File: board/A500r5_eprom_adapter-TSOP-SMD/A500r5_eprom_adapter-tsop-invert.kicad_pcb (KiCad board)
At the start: 4 copper layers, 17.4 x 50.9 mm, 13 parts, among them J2 A18 Selector, J4 A17 Selector, U1 27C400-A500, U2 SST39SF040_TSOP, U3 SST39SF040_TSOP

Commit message: Update the README
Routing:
- net GND: track 65.7 -> 69.8 mm
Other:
- board text added: "Rev. 1"
- board text removed: "Rev. 0"
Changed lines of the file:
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@@
 		)
 	)
-	(gr_text "Rev. 0"
+	(gr_text "Rev. 1"
 		(at 112.268 124.206 90)
 		(layer "F.SilkS")
@@
 	)
 	(segment
-		(start 117.3124 112.9736)
-		(end 117.3124 115.7884)
+		(start 118.115 112.171)
+		(end 115.921 112.171)
 		(width 0.25)
 		(layer "F.Cu")
@@
 	)
 	(segment
-		(start 117.3124 115.7884)
-		(end 118.11 116.586)
+		(start 115.57 116.332)
+		(end 115.57 112.522)
 		(width 0.25)
 		(layer "F.Cu")
@@
 	)
 	(segment
-		(start 118.115 112.171)
-		(end 117.3124 112.9736)
+		(start 118.11 116.586)
+		(end 115.824 116.586)
 		(width 0.25)
 		(layer "F.Cu")
+		(net 1)
+	)
+	(segment
+		(start 115.824 116.586)
+		(end 115.57 116.332)
+		(width 0.25)
+		(layer "F.Cu")
+		(net 1)
+	)
+	(segment
+		(start 115.921 112.171)
+		(end 115.57 112.522)
+		(width 0.25)
+		(layer "F.Cu")

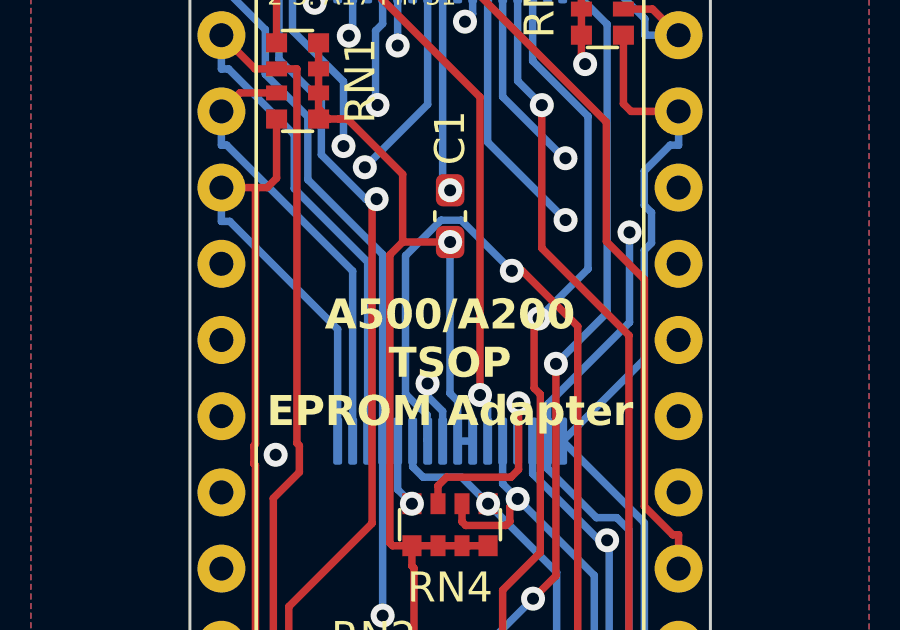
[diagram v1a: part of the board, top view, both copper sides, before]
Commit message: Fix "A2000" silkscreen in PLCC and TSOP adapter variants
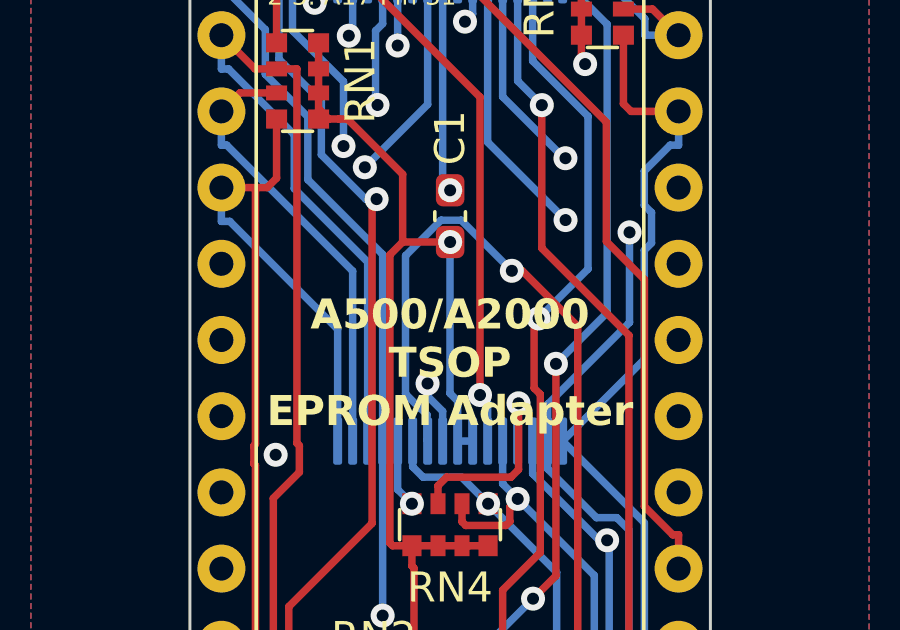
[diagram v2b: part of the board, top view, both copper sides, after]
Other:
- board text added: "A500/A2000 TSOP EPROM Adapter"
- board text removed: "A500/A200 TSOP EPROM Adapter"
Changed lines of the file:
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@@
 			(drillshape 0)
 			(scaleselection 1)
-			(outputdirectory "gerbers/rev0/")
+			(outputdirectory "gerbers/rev1/")
 		)
 	)
@@
 		)
 	)
-	(gr_text "A500/A200\nTSOP\nEPROM Adapter"
+	(gr_text "A500/A2000\nTSOP\nEPROM Adapter"
 		(at 118.11 90.932 0)
 		(layer "F.SilkS")
